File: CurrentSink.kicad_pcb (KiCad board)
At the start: 2 copper layers, 45 x 50 mm, 23 parts, among them J101 Tst, J102 pwrJmp, J103 Pwr, Q301 STP55NF06L, U201 MCP6002, U401 TPS7A2401

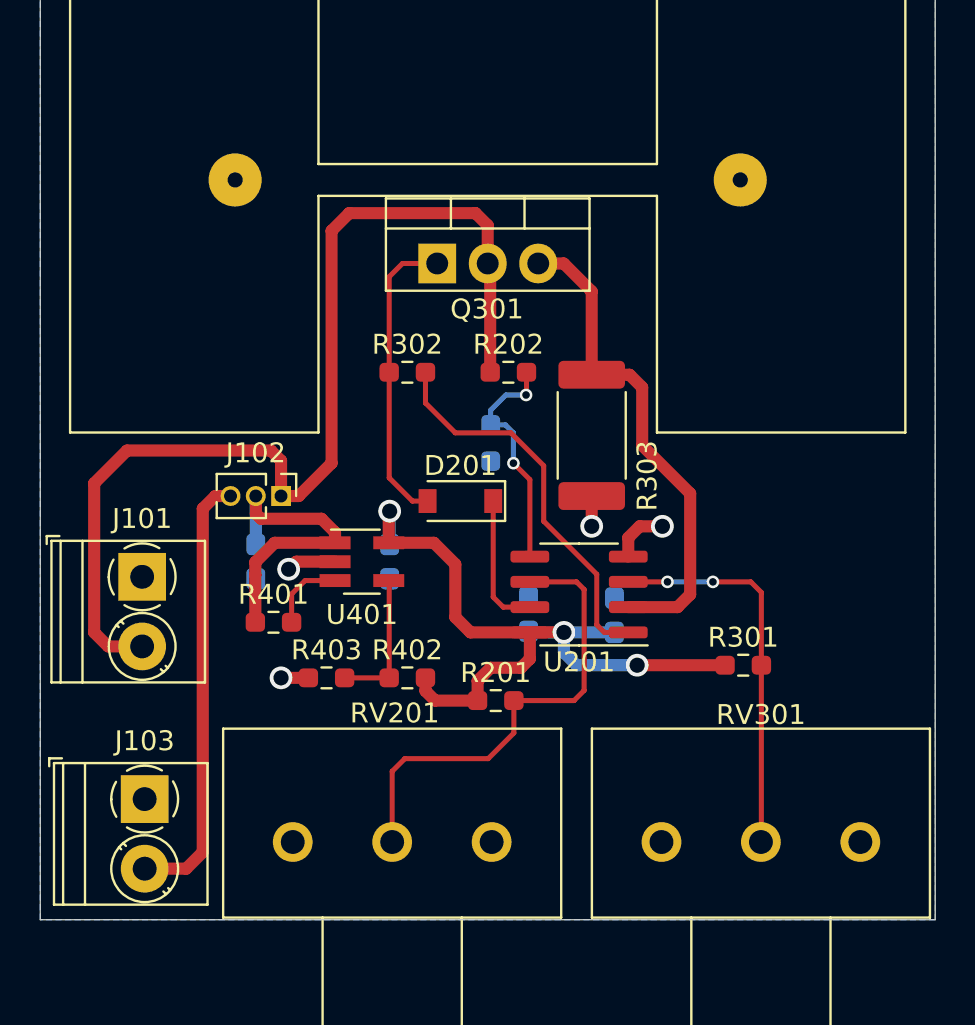
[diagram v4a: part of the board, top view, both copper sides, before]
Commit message: All component placements complete, silk screen cleaned up, and tracks routed. DRC passed.
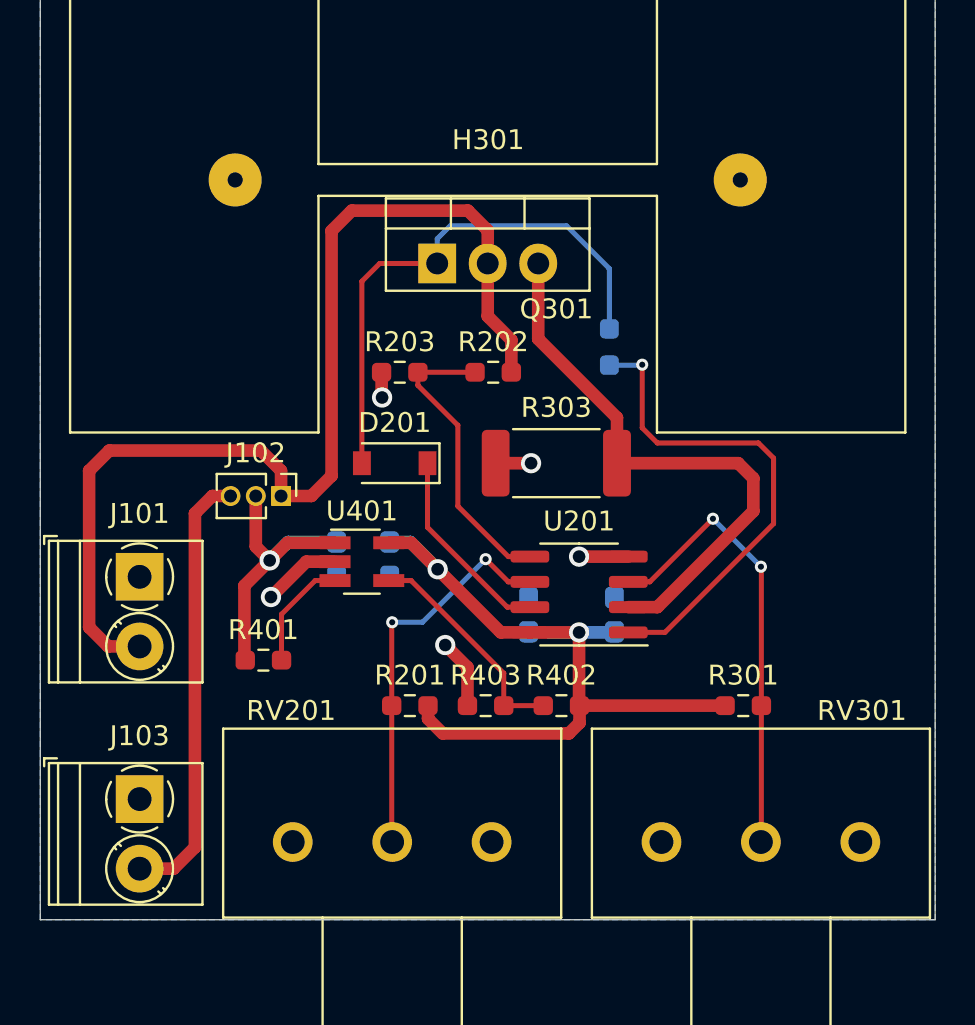
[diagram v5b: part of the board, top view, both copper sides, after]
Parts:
- R203: moved to F.Cu
- R302: moved to B.Cu
- moved R302 10.2 mm to (118.6, 76.2), turned to 270 degrees
- moved R403 8.12 mm to (112.4, 94.2)
- moved R402 7.87 mm to (116.2, 94.2)
- moved R203 5.79 mm to (108.1, 77.5), turned to 180 degrees
- moved R201 4.33 mm to (108.6, 94.2), turned to 180 degrees
- moved C401 4.07 mm to (104.9, 86.9)
- moved D201 3.81 mm to (107.8, 82.0)
- moved R303 2.26 mm to (116.0, 82.0), turned to 180 degrees
- moved R301 2.03 mm to (125.3, 94.2)
- moved R401 1.97 mm to (101.2, 91.9)
- moved R202 0.76 mm to (112.8, 77.5), turned to 180 degrees
- moved J103 0.25 mm to (95.0, 98.9)
- moved C404 0.13 mm to (107.6, 86.9)
- moved J101 0.13 mm to (95.0, 87.8)
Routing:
- net /Vctrl: track 15.2 -> 27.4 mm
- net Net-(R302-Pad2): track 19.6 -> 24.9 mm, vias 0 -> 1
- net GND: track 8.29 -> 13.0 mm, vias 4 -> 5
- net /Power-Reg/regFB: track 7.14 -> 11.4 mm
- net Net-(R201-Pad2): track 23.8 -> 19.8 mm, vias 0 -> 2
- net Net-(Q301-Pad3): track 25.1 -> 28.8 mm
- net Net-(R301-Pad2): track 19.5 -> 22.7 mm
- net Net-(D201-Pad1): track 6.88 -> 10.0 mm
- net Net-(R202-Pad2): track 12.1 -> 15.1 mm, vias 2 -> 0
- net /Power-Reg/regEN: track 3.88 -> 5.70 mm
- net /2.5V: track 38.1 -> 39.5 mm, vias 3 -> 2
- net /tstV+: track 53.1 -> 54.2 mm
- net /regIN: track 16.0 -> 16.5 mm, vias 0 -> 1
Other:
- net class Default: clearance 0.2032 -> 0.254; via_dia 0.635 -> 0.6096; via_drill 0.381 -> 0.3048
- net class Power: clearance 0.1524 -> 0.254; trace_width 0.6096 -> 0.635; via_dia 1.143 -> 1.016; via_drill 0.762 -> 0.635
- rule trace_clearance: 0.2032 -> 0.254
- rule via_min_size: 0.4064 -> 0.3048

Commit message: Revision A as sent to OSHPark with some MPN updates due to availability
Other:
- board text added: "Current Sink or Swim"
- board text added: "Designed By: Nathan S."
